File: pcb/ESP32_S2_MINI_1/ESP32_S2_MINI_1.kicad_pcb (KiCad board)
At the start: 4 copper layers, 22.9 x 50.8 mm, 50 parts, among them J1 USB_C_Receptacle_USB2.0, J2 Conn_01x12_Female, J3 Conn_01x16_Female, J4 Conn_01x02_Female, J5 STEMMA, Q1 DMG3415u, U1 AP2112K-3.3, U2 ESP32-S2-MINI-1, U3 LTR-329ALS-01, U4 MT8691AT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

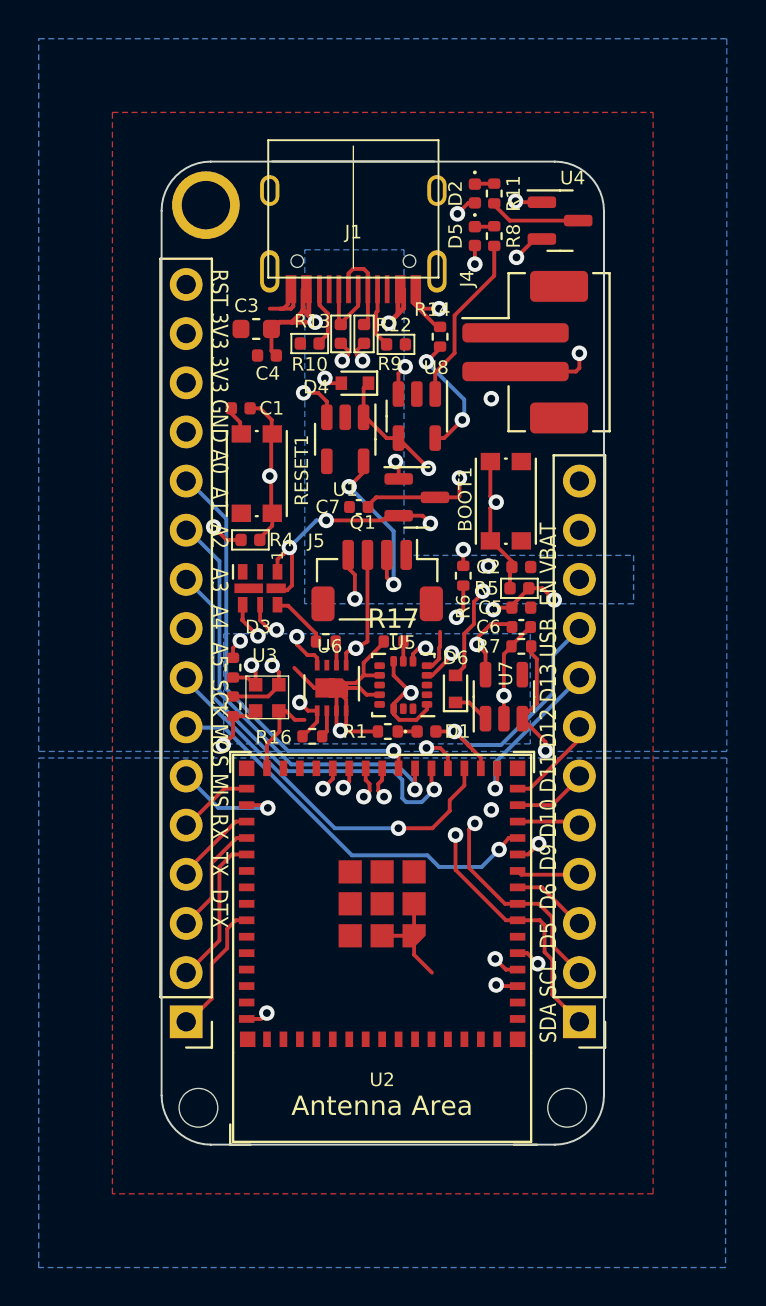
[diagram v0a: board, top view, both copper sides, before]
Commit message: Version 1.1, see Errata for fixes
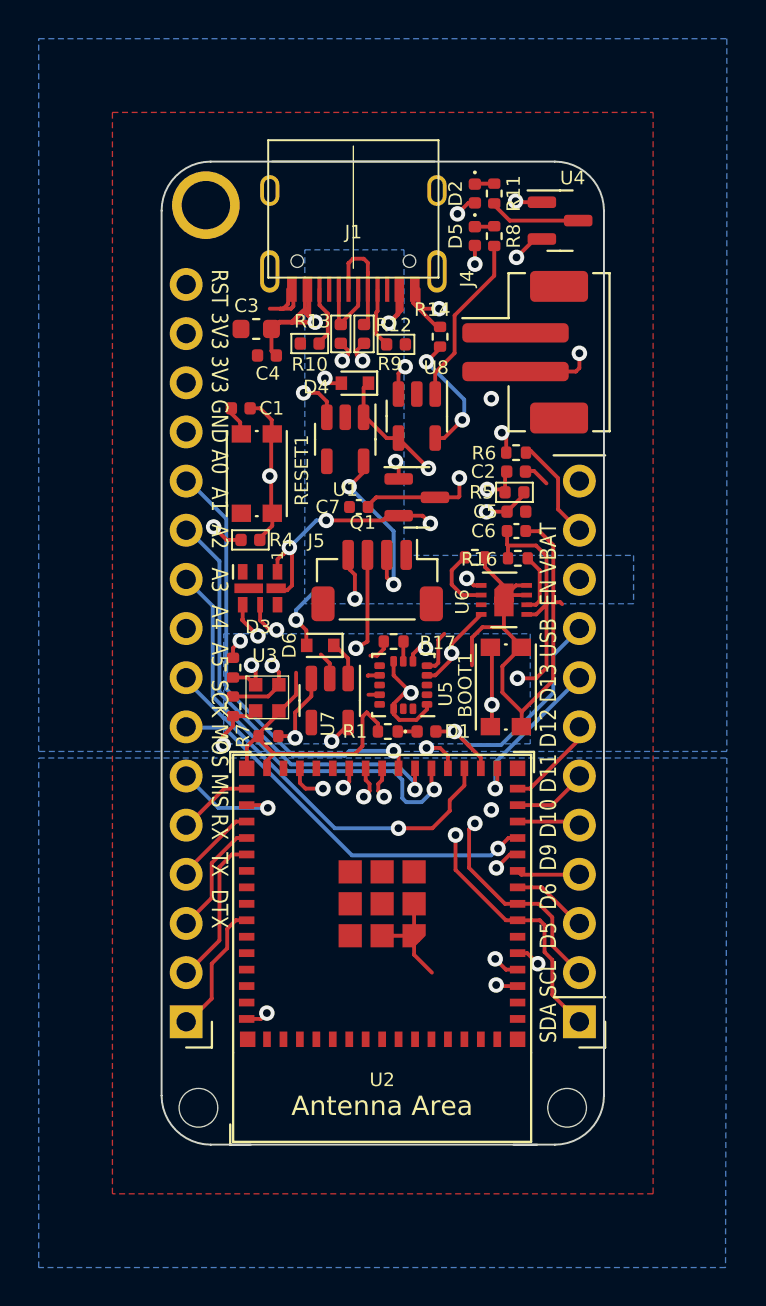
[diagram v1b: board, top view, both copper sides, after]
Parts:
- moved R16 14.1 mm to (200.0, 77.7)
- moved R7 13.9 mm to (187.1, 86.8)
- moved U6 10.00 mm to (199.3, 79.8), turned to 0 degrees
- moved BOOT1 9.60 mm to (199.4, 84.3)
- moved U7 9.00 mm to (190.3, 85.0), turned to -90 degrees
- moved R15 8.84 mm to (197.8, 77.6), turned to 180 degrees
- moved D6 7.34 mm to (189.8, 82.2), turned to 180 degrees
- moved R6 6.92 mm to (199.9, 72.2), turned to 180 degrees
- moved C5 4.97 mm to (199.9, 75.2)
- moved C6 4.97 mm to (199.9, 76.2)
- moved R5 4.97 mm to (199.8, 74.2)
- moved C2 4.94 mm to (199.9, 73.2)
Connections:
- U2 pad 26: /APA_DATA -> unconnected-(U2-Pad26)
- U2 pad 28: unconnected-(U2-Pad28) -> /APA_DATA
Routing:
- net GND: track 51.1 -> 70.9 mm, vias 5 -> 2
- net I2C_PWR: track 12.8 -> 21.6 mm
- net +3.3VA: track 23.0 -> 29.8 mm
- net /BOOT: track 33.1 -> 38.1 mm, vias 2 -> 3
- net EN: track 23.4 -> 28.0 mm, vias 2 -> 1
- net I2C_SDA: track 43.9 -> 48.1 mm, vias 4 -> 5
- net /VB: track 21.9 -> 25.8 mm
- net Net-(R15-Pad2): track 1.25 -> 3.39 mm
- net Net-(R16-Pad2): track 1.43 -> 3.22 mm
- net USB: track 19.4 -> 18.1 mm
- net +3V3: track 18.6 -> 19.7 mm, vias 8 -> 7
- net /DN: track 4.80 -> 5.84 mm
- net /APA_DATA: track 12.6 -> 13.4 mm
- net I2C_SCL: track 42.8 -> 43.4 mm, vias 5 -> 4
- net A5: track 20.7 -> 20.2 mm

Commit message: S3 version
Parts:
- U2: value ESP32-S2-MINI-1 -> ESP32-S3-MINI-1
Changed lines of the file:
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@@
 (kicad_pcb (version 20211014) (generator pcbnew)
   (general
-    (thickness 4.69)
+    (thickness 1.69)
   )
   (paper "A4")
@@
       (layer "F.Mask" (type "Top Solder Mask") (color "Green") (thickness 0.01))
       (layer "F.Cu" (type "copper") (thickness 0.035))
-      (layer "dielectric 1" (type "core") (thickness 1.51) (material "FR4") (epsilon_r 4.5) (loss_tangent 0.02))
+      (layer "dielectric 1" (type "core") (thickness 0.51) (material "FR4") (epsilon_r 4.5) (loss_tangent 0.02))
       (layer "In1.Cu" (type "copper") (thickness 0.035))
-      (layer "dielectric 2" (type "prepreg") (thickness 1.51) (material "FR4") (epsilon_r 4.5) (loss_tangent 0.02))
+      (layer "dielectric 2" (type "prepreg") (thickness 0.51) (material "FR4") (epsilon_r 4.5) (loss_tangent 0.02))
       (layer "In2.Cu" (type "copper") (thickness 0.035))
-      (layer "dielectric 3" (type "core") (thickness 1.51) (material "FR4") (epsilon_r 4.5) (loss_tangent 0.02))
+      (layer "dielectric 3" (type "core") (thickness 0.51) (material "FR4") (epsilon_r 4.5) (loss_tangent 0.02))
       (layer "B.Cu" (type "copper") (thickness 0.035))
       (layer "B.Mask" (type "Bottom Solder Mask") (color "Green") (thickness 0.01))
@@
       (drillshape 0)
       (scaleselection 1)
-      (outputdirectory "Sep2022")
+      (outputdirectory "Nov2022")
     )
   )
@@
     (descr "http://www.diodes.com/datasheets/ap02001.pdf p.144")
     (tags "Diode SOD523")
+    (property "MFGR" "Shikues")
     (property "MPN" "MSK4005")
     (property "Sheetfile" "ESP32_S2_MINI_1.kicad_sch")
@@
     (descr "ESP32-S2-MINI-1 and ESP32-S2-MINI-1U: https://www.espressif.com/sites/default/files/documentation/esp32-s2-mini-1_esp32-s2-mini-1u_datasheet_en.pdf")
     (tags "ESP32-S2")
+    (property "MFGR" "Espressif Systems")
+    (property "MPN" "ESP32-S3-MINI-1-N8")
     (property "Sheetfile" "ESP32_S2_MINI_1.kicad_sch")
     (property "Sheetname" "")
@@
       (effects (font (size 0.7 0.7) (thickness 0.1)))
     )
-    (fp_text value "ESP32-S2-MINI-1" (at 0 9.4) (layer "F.Fab")
+    (fp_text value "ESP32-S3-MINI-1" (at 0 9.4) (layer "F.Fab")
       (effects (font (size 1 1) (thickness 0.15)))
     )
@@
     (descr "SOT, 5 Pin (https://www.jedec.org/sites/default/files/docs/Mo-178c.PDF variant AA), generated with kicad-footprint-generator ipc_gullwing_generator.py")
     (tags "SOT TO_SOT_SMD")
+    (property "MFGR" "Diodes Incorporated")
+    (property "MPN" "AP2112K-3.3TRG1")
     (property "Sheetfile" "ESP32_S2_MINI_1.kicad_sch")
     (property "Sheetname" "")
@@
     (descr "LGA, 16 Pin (http://www.st.com/resource/en/datasheet/lis331hh.pdf), generated with kicad-footprint-generator ipc_noLead_generator.py")
     (tags "LGA NoLead")
+    (property "MFGR" "ST")
+    (property "MPN" "LIS3DH")
     (property "Sheetfile" "ESP32_S2_MINI_1.kicad_sch")
     (property "Sheetname" "")
@@
   (footprint "ToyTronics:LTR-329ALS-01" (layer "F.Cu")
     (at 187.071 84.836)
+    (property "MFGR" "Lite-On")
+    (property "MPN" "LTR-329ALS-01")
     (property "Sheetfile" "ESP32_S2_MINI_1.kicad_sch")
     (property "Sheetname" "")
@@
     (descr "Sensirion DFN-8 SHT3x-DIS (https://www.sensirion.com/fileadmin/user_upload/customers/sensirion/Dokumente/2_Humidity_Sensors/Datasheets/Sensirion_Humidity_Sensors_SHT3x_Datasheet_digital.pdf)")
     (tags "sensirion dfn nolead")
+    (property "MFGR" "Sensiron")
+    (property "MPN" "SHT31-DIS")
     (property "Sheetfile" "ESP32_S2_MINI_1.kicad_sch")
     (property "Sheetname" "")
@@
     (descr "SOT, 3 Pin (https://www.jedec.org/system/files/docs/to-236h.pdf variant AB), generated with kicad-footprint-generator ipc_gullwing_generator.py")
     (tags "SOT TO_SOT_SMD")
+    (property "MFGR" "Diodes Incorporated")
+    (property "MPN" "DMG3415U-7")
     (property "Sheetfile" "ESP32_S2_MINI_1.kicad_sch")
     (property "Sheetname" "")
@@
     (descr "http://www.led-color.com/upload/201604/APA102-2020%20SMD%20LED.pdf")
     (tags "LED RGB SPI")
+    (property "MFGR" "Shenzhen LED Color Co.,LTD")
+    (property "MPN" "LC8822-2020-6")
     (property "Sheetfile" "ESP32_S2_MINI_1.kicad_sch")
     (property "Sheetname" "")
@@
     (pad "6" smd rect (at 0 0.59) (size 1.48 0.5) (layers "F.Cu" "F.Paste" "F.Mask")
       (net 2 "GND") (pinfunction "GND") (pintype "power_in"))
-    (model "${KICAD6_3DMODEL_DIR}/LED_SMD.3dshapes/LED-APA102-2020.wrl"
-      (offset (xyz 0 0 0))
-      (scale (xyz 1 1 1))
-      (rotate (xyz 0 0 0))
+    (model "${KICAD6_3DMODEL_DIR}/LED_SMD.3dshapes/APA102 2020 LED.step"
+      (offset (xyz 0 0 0))
+      (scale (xyz 1 1 1))
+      (rotate (xyz -90 0 0))
     )
   )
@@
       (net 58 "RST") (pinfunction "Pin_16") (pintype "passive"))
     (model "${KICAD6_3DMODEL_DIR}/Connector_PinHeader_2.54mm.3dshapes/PinHeader_1x16_P2.54mm_Vertical.wrl"
-      (offset (xyz 0 0 0))
-      (scale (xyz 1 1 1))
-      (rotate (xyz 0 0 0))
+      (offset (xyz 0 0 -2))
+      (scale (xyz 1 1 1))
+      (rotate (xyz 0 180 0))
     )
   )
@@
     (pad "MP" smd roundrect (at -2.8 -1.2 180) (size 1.2 1.8) (layers "F.Cu" "F.Paste" "F.Mask") (roundrect_rratio 0.2083333333))
     (pad "MP" smd roundrect (at 2.8 -1.2 180) (size 1.2 1.8) (layers "F.Cu" "F.Paste" "F.Mask") (roundrect_rratio 0.2083333333))
-    (model "${KICAD6_3DMODEL_DIR}/Connector_JST.3dshapes/JST_SH_BM04B-SRSS-TB_1x04-1MP_P1.00mm_Vertical.wrl"
-      (offset (xyz 0 0 0))
-      (scale (xyz 1 1 1))
-      (rotate (xyz 0 0 0))
+    (model "${KICAD6_3DMODEL_DIR}/Connector_JST.3dshapes/BM04B-SRSS-TB-LF--SN---3DModel-STEP-56544.STEP"
+      (offset (xyz 0 0 0))
+      (scale (xyz 1 1 1))
+      (rotate (xyz -90 0 0))
     )
   )
@@
     (pad "2" smd rect (at -2.05 0.8 270) (size 0.9 1) (layers "F.Cu" "F.Paste" "F.Mask")
       (net 2 "GND") (pinfunction "2") (pintype "passive"))
-    (model "${KICAD6_3DMODEL_DIR}/Button_Switch_SMD.3dshapes/SW_Push_1P1T_NO_CK_KMR2.wrl"
-      (offset (xyz 0 0 0))
-      (scale (xyz 1 1 1))
-      (rotate (xyz 0 0 0))
+    (model "${KICAD6_3DMODEL_DIR}/Button_Switch_SMD.3dshapes/KMR221GLFS--3DModel-STEP-56544.STEP"
+      (offset (xyz 0 0 1.4))
+      (scale (xyz 1 1 1))
+      (rotate (xyz -90 0 0))
     )
   )
@@
       (net 29 "VBAT") (pinfunction "Pin_12") (pintype "passive"))
     (model "${KICAD6_3DMODEL_DIR}/Connector_PinHeader_2.54mm.3dshapes/PinHeader_1x12_P2.54mm_Vertical.wrl"
-      (offset (xyz 0 0 0))
-      (scale (xyz 1 1 1))
-      (rotate (xyz 0 0 0))
+      (offset (xyz 0 0 -2))
+      (scale (xyz 1 1 1))
+      (rotate (xyz 0 180 0))
     )
   )
@@
     (pad "2" smd rect (at 2.05 0.8 90) (size 0.9 1) (layers "F.Cu" "F.Paste" "F.Mask")
       (net 2 "GND") (pinfunction "2") (pintype "passive"))
-    (model "${KICAD6_3DMODEL_DIR}/Button_Switch_SMD.3dshapes/SW_Push_1P1T_NO_CK_KMR2.wrl"
-      (offset (xyz 0 0 0))
-      (scale (xyz 1 1 1))
-      (rotate (xyz 0 0 0))
+    (model "${KICAD6_3DMODEL_DIR}/Button_Switch_SMD.3dshapes/KMR221GLFS--3DModel-STEP-56544.STEP"
+      (offset (xyz 0 0 1.4))
+      (scale (xyz 1 1 1))
+      (rotate (xyz -90 0 0))
     )
   )
@@
     (descr "SOT, 5 Pin (https://www.jedec.org/sites/default/files/docs/Mo-178c.PDF variant AA), generated with kicad-footprint-generator ipc_gullwing_generator.py")
     (tags "SOT TO_SOT_SMD")
+    (property "MFGR" "Microchip Technology")
+    (property "MPN" "MCP73831T-4ADI/OT")
     (property "Sheetfile" "ESP32_S2_MINI_1.kicad_sch")
     (property "Sheetname" "")
@@
     (descr "http://www.diodes.com/datasheets/ap02001.pdf p.144")
     (tags "Diode SOD523")
+    (property "MFGR" "Shikues")
     (property "MPN" "MSK4005")
     (property "Sheetfile" "ESP32_S2_MINI_1.kicad_sch")
@@
     (descr "SOT, 5 Pin (https://www.jedec.org/sites/default/files/docs/Mo-178c.PDF variant AA), generated with kicad-footprint-generator ipc_gullwing_generator.py")
     (tags "SOT TO_SOT_SMD")
+    (property "MFGR" "Diodes Incorporated")
+    (property "MPN" "AP2112K-3.3TRG1")
     (property "Sheetfile" "ESP32_S2_MINI_1.kicad_sch")
     (property "Sheetname" "")
@@
     (descr "SOT, 3 Pin (https://www.jedec.org/system/files/docs/to-236h.pdf variant AB), generated with kicad-footprint-generator ipc_gullwing_generator.py")
     (tags "SOT TO_SOT_SMD")
+    (property "MFGR" "Honeywell")
     (property "MPN" "MT8691AT")
     (property "Sheetfile" "ESP32_S2_MINI_1.kicad_sch")
@@
     (at 191.520032 58.645268 180)
     (descr "Korean Hroparts Elec, Power only USB connector supporting up to 3A")
+    (property "MFGR" "Korean Hroparts Elec")
+    (property "MPN" "TYPE-C-31-M-12")
     (property "Sheetfile" "ESP32_S2_MINI_1.kicad_sch")
     (property "Sheetname" "")
@@
     (pad "S1" thru_hole roundrect (at -4.32 -4.18 180) (size 1 2.2) (drill oval 0.6 1.7) (layers *.Cu *.Mask) (roundrect_rratio 0.5)
       (net 2 "GND") (pinfunction "SHIELD") (pintype "passive"))
+    (model "${KICAD6_3DMODEL_DIR}/USB-C-connectors.3dshapes/HRO  TYPE-C-31-M-12.step"
+      (offset (xyz -4.5 -2.6 0))
+      (scale (xyz 1 1 1))
+      (rotate (xyz -90 0 0))
+    )
   )
   (footprint "Resistor_SMD:R_0402_1005Metric" (layer "F.Cu")
